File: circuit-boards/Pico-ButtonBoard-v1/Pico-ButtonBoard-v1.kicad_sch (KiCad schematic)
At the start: 16 parts, among them J17 CAN, J18 CAN, J19 BATT, J22 DC_IN, U3 MCP2518FDT-H/SL, U4 MCP2558FD, U5 4.0 MHz

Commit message: Update footprints
Signed-off-by: Scott Berman <sgberman1@gmail.com>
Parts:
- TP101: renamed from TP1; footprint (none) -> TestPoint:TestPoint_Keystone_5000-5004_Miniature; now not fitted
- TP102: renamed from TP2; footprint (none) -> TestPoint:TestPoint_Keystone_5000-5004_Miniature; now not fitted
- U101: renamed from U5; footprint (none) -> Pico-ButtonBoard:Wurth-CFPS-73
- renumbered A1 to A101, C19 to C101, C23 to C102, C20 to C103, C21 to C104, C22 to C105, J22 to J101, J19 to J102, J17 to J103, J18 to J104, R49 to R101, U3 to U102, U4 to U103
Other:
- title: (none) -> Pico Button Board

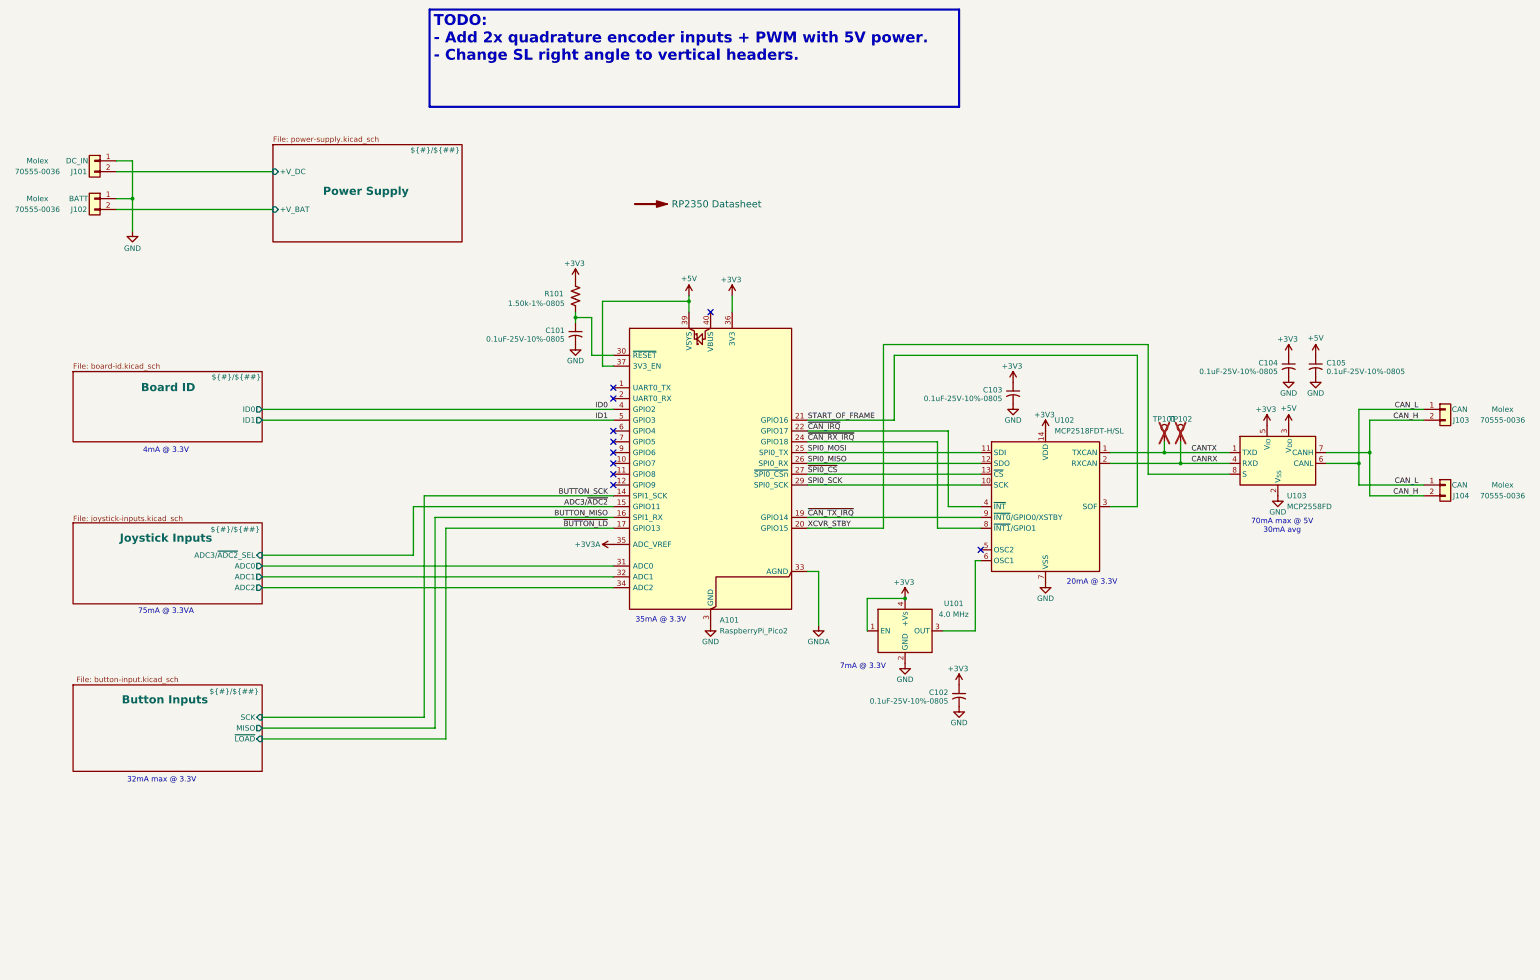
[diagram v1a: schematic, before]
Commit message: Pico Button Board initial placement
Signed-off-by: Scott Berman <sgberman1@gmail.com>
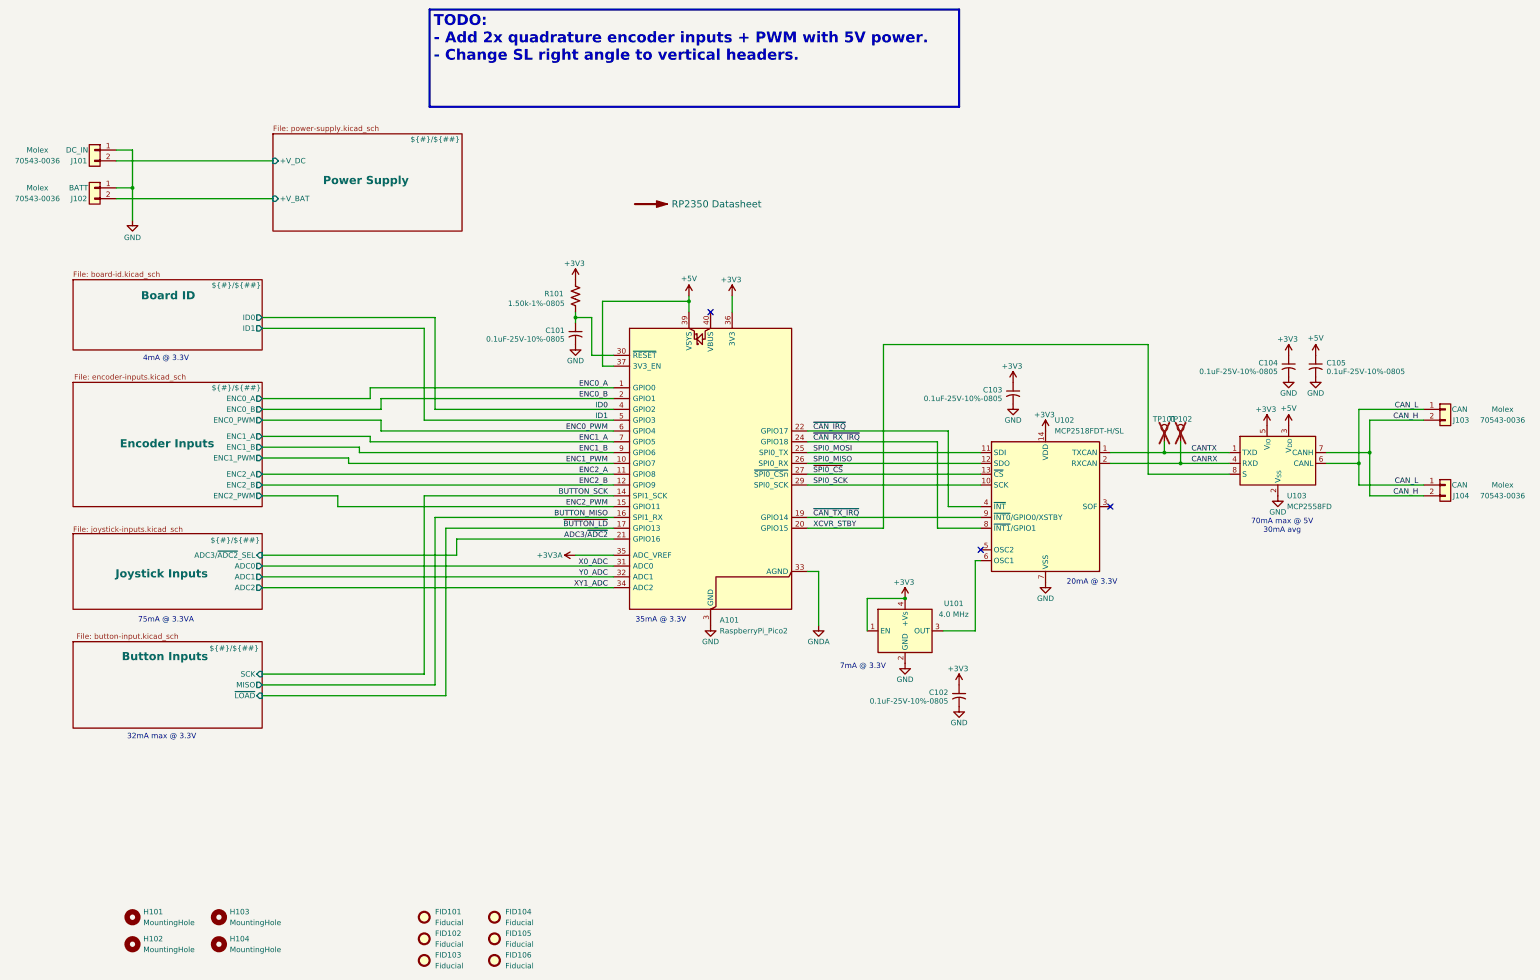
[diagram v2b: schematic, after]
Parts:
- added FID101, FID102, FID103, FID104, FID105, FID106: Fiducial, Fiducial:Fiducial_Cross_1.5mm_Mask2mm, symbol Mechanical:Fiducial
- added H101, H102, H103, H104: MountingHole, MountingHole:MountingHole_3.2mm_M3, symbol Mechanical:MountingHole
- C101, C102, C103, C104, C105: LCSC Part # C519981 -> (none)
- J101, J102, J103, J104: footprint Pico-ButtonBoard:Molex-70555-0036 -> Pico-ButtonBoard:Molex-70543-0001; DIST P/N WM4175-ND -> WM4824-ND; MFG P/N 70555-0036 -> 70543-0036
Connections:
- net ADC3/~{ADC2}: now also A101.21 (GPIO16); no longer A101.15 (GPIO11)
- net ENC0_A: now reaches A101.1 (GPIO0)
- net ENC1_PWM: now reaches A101.10 (GPIO7)
- net ENC2_A: now reaches A101.11 (GPIO8)
- net ENC2_B: now reaches A101.12 (GPIO9)
- net ENC0_B: now reaches A101.2 (GPIO1)
- net ENC0_PWM: now reaches A101.6 (GPIO4)
- net ENC1_A: now reaches A101.7 (GPIO5)
- net ENC1_B: now reaches A101.9 (GPIO6)
- net Joystick Inputs/ADC0 renamed X0_ADC
- net Joystick Inputs/ADC1 renamed Y0_ADC
- net Joystick Inputs/ADC2 renamed XY1_ADC
- net START_OF_FRAME: no longer names the net of U102.3 (CLKO/SOF)
- net START_OF_FRAME: no longer A101.21 (GPIO16)
- new net ENC2_PWM: A101.15 (GPIO11)
- no-connect marks 10 -> 3
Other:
- added sheet Encoder Inputs (encoder-inputs.kicad_sch)
- moved on the sheet: J101, J102

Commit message: Pico Button Board initial pcb checkin
Signed-off-by: Scott Berman <sgberman1@gmail.com>
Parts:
- A1: renamed from A101; footprint Module:RaspberryPi_Pico_Common_Unspecified -> Pico-ButtonBoard:RaspberryPi_Pico_Common_Unspecified
- FID1: renamed from FID105; footprint Fiducial:Fiducial_Cross_1.5mm_Mask2mm -> Pico-ButtonBoard:Fiducial_1.6mm_Mask3mm
- FID2: renamed from FID103; footprint Fiducial:Fiducial_Cross_1.5mm_Mask2mm -> Pico-ButtonBoard:Fiducial_1.6mm_Mask3mm
- FID3: renamed from FID101; footprint Fiducial:Fiducial_Cross_1.5mm_Mask2mm -> Pico-ButtonBoard:Fiducial_1.6mm_Mask3mm
- FID4: renamed from FID102; footprint Fiducial:Fiducial_Cross_1.5mm_Mask2mm -> Pico-ButtonBoard:Fiducial_1.6mm_Mask3mm
- FID5: renamed from FID104; footprint Fiducial:Fiducial_Cross_1.5mm_Mask2mm -> Pico-ButtonBoard:Fiducial_1.6mm_Mask3mm
- FID6: renamed from FID106; footprint Fiducial:Fiducial_Cross_1.5mm_Mask2mm -> Pico-ButtonBoard:Fiducial_1.6mm_Mask3mm
- renumbered C104 to C20, C105 to C22, C103 to C23, C101 to C26, C102 to C4, H101 to H1, H102 to H2, H104 to H3, H103 to H4, J104 to J19, J103 to J20, J102 to J21, J101 to J22, R101 to R59, TP101 to TP4, TP102 to TP5, U101 to U4, U102 to U5, U103 to U8
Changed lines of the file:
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@@
 		)
 	)
-	(text_box "TODO:\n- Add 2x quadrature encoder inputs + PWM with 5V power.\n- Change SL right angle to vertical headers."
-		(exclude_from_sim no)
-		(at 138.43 27.94 0)
-		(size 124.46 22.86)
-		(margins 0.9525 0.9525 0.9525 0.9525)
-		(stroke
-			(width 0.508)
-			(type solid)
-			(color 255 0 0 1)
-		)
-		(fill
-			(type none)
-		)
-		(effects
-			(font
-				(size 2.54 2.54)
-				(thickness 0.508)
-				(bold yes)
-				(color 255 0 0 1)
-			)
-			(justify left top)
-		)
-	)
 	(junction
 		(at 250.19 166.37)
@@
 		(dnp no)
 		(fields_autoplaced yes)
-		(property "Reference" "H103"
+		(property "Reference" "H4"
 			(at 91.44 240.0299 0)
 			(effects
@@
 			(project "Pico-ButtonBoard-v1"
 				(path "/644201a9-3a2f-4df3-9c93-2ae55394df4b"
-					(reference "H103")
+					(reference "H4")
 					(unit 1)
 				)
@@
 		(dnp no)
 		(fields_autoplaced yes)
-		(property "Reference" "FID103"
+		(property "Reference" "FID2"
 			(at 139.7 250.1899 0)
 			(effects
@@
 			)
 		)
-		(property "Footprint" "Fiducial:Fiducial_Cross_1.5mm_Mask2mm"
+		(property "Footprint" "Pico-ButtonBoard:Fiducial_1.6mm_Mask3mm"
 			(at 137.16 251.46 0)
 			(effects
@@
 			(project "Pico-ButtonBoard-v1"
 				(path "/644201a9-3a2f-4df3-9c93-2ae55394df4b"
-					(reference "FID103")
+					(reference "FID2")
 					(unit 1)
 				)
@@
 		(dnp no)
 		(fields_autoplaced yes)
-		(property "Reference" "FID104"
+		(property "Reference" "FID5"
 			(at 156.21 240.0299 0)
 			(effects
@@
 			)
 		)
-		(property "Footprint" "Fiducial:Fiducial_Cross_1.5mm_Mask2mm"
+		(property "Footprint" "Pico-ButtonBoard:Fiducial_1.6mm_Mask3mm"
 			(at 153.67 241.3 0)
 			(effects
@@
 			(project "Pico-ButtonBoard-v1"
 				(path "/644201a9-3a2f-4df3-9c93-2ae55394df4b"
-					(reference "FID104")
+					(reference "FID5")
 					(unit 1)
 				)
@@
 		(on_board yes)
 		(dnp no)
-		(property "Reference" "C104"
+		(property "Reference" "C20"
 			(at 337.82 110.998 0)
 			(effects
@@
 			(project "Pico-ButtonBoard-v1"
 				(path "/644201a9-3a2f-4df3-9c93-2ae55394df4b"
-					(reference "C104")
+					(reference "C20")
 					(unit 1)
 				)
@@
 		(dnp no)
 		(fields_autoplaced yes)
-		(property "Reference" "FID102"
+		(property "Reference" "FID4"
 			(at 139.7 245.1099 0)
 			(effects
@@
 			)
 		)
-		(property "Footprint" "Fiducial:Fiducial_Cross_1.5mm_Mask2mm"
+		(property "Footprint" "Pico-ButtonBoard:Fiducial_1.6mm_Mask3mm"
 			(at 137.16 246.38 0)
 			(effects
@@
 			(project "Pico-ButtonBoard-v1"
 				(path "/644201a9-3a2f-4df3-9c93-2ae55394df4b"
-					(reference "FID102")
+					(reference "FID4")
 					(unit 1)
 				)
@@
 		(on_board yes)
 		(dnp no)
-		(property "Reference" "J101"
+		(property "Reference" "J22"
 			(at 57.912 63.5 0)
 			(effects
@@
 			(project "Pico-ButtonBoard-v1"
 				(path "/644201a9-3a2f-4df3-9c93-2ae55394df4b"
-					(reference "J101")
+					(reference "J22")
 					(unit 1)
 				)
@@
 		(dnp no)
 		(fields_autoplaced yes)
-		(property "Reference" "FID105"
+		(property "Reference" "FID1"
 			(at 156.21 245.1099 0)
 			(effects
@@
 			)
 		)
-		(property "Footprint" "Fiducial:Fiducial_Cross_1.5mm_Mask2mm"
+		(property "Footprint" "Pico-ButtonBoard:Fiducial_1.6mm_Mask3mm"
 			(at 153.67 246.38 0)
 			(effects
@@
 			(project "Pico-ButtonBoard-v1"
 				(path "/644201a9-3a2f-4df3-9c93-2ae55394df4b"
-					(reference "FID105")
+					(reference "FID1")
 					(unit 1)
 				)
@@
 		(dnp no)
 		(fields_autoplaced yes)
-		(property "Reference" "H104"
+		(property "Reference" "H3"
 			(at 91.44 246.3799 0)
 			(effects
@@
 			(project "Pico-ButtonBoard-v1"
 				(path "/644201a9-3a2f-4df3-9c93-2ae55394df4b"
-					(reference "H104")
+					(reference "H3")
 					(unit 1)
 				)
@@
 		(dnp no)
 		(fields_autoplaced yes)
-		(property "Reference" "A101"
+		(property "Reference" "A1"
 			(at 206.6133 171.45 0)
 			(effects
@@
 			)
 		)
-		(property "Footprint" "Module:RaspberryPi_Pico_Common_Unspecified"
+		(property "Footprint" "Pico-ButtonBoard:RaspberryPi_Pico_Common_Unspecified"
 			(at 204.47 184.15 0)
 			(effects
@@
 			(project ""
 				(path "/644201a9-3a2f-4df3-9c93-2ae55394df4b"
-					(reference "A101")
+					(reference "A1")
 					(unit 1)
 				)
@@
 		(on_board yes)
 		(dnp no)
-		(property "Reference" "J103"
+		(property "Reference" "J20"
 			(at 378.968 124.46 0)
 			(effects
@@
 			(project "Pico-ButtonBoard-v1"
 				(path "/644201a9-3a2f-4df3-9c93-2ae55394df4b"
-					(reference "J103")
+					(reference "J20")
 					(unit 1)
 				)
@@
 		(on_board yes)
 		(dnp no)
-		(property "Reference" "C105"
+		(property "Reference" "C22"
 			(at 349.25 110.998 0)
 			(effects
@@
 			(project "Pico-ButtonBoard-v1"
 				(path "/644201a9-3a2f-4df3-9c93-2ae55394df4b"
-					(reference "C105")
+					(reference "C22")
 					(unit 1)
 				)
@@
 		(on_board yes)
 		(dnp no)
-		(property "Reference" "R101"
+		(property "Reference" "R59"
 			(at 169.926 94.742 0)
 			(effects
@@
 			(project "Pico-ButtonBoard-v1"
 				(path "/644201a9-3a2f-4df3-9c93-2ae55394df4b"
-					(reference "R101")
+					(reference "R59")
 					(unit 1)
 				)
@@
 		(on_board yes)
 		(dnp no)
-		(property "Reference" "C101"
+		(property "Reference" "C26"
 			(at 170.18 103.378 0)
 			(effects
@@
 			(project "Pico-ButtonBoard-v1"
 				(path "/644201a9-3a2f-4df3-9c93-2ae55394df4b"
-					(reference "C101")
+					(reference "C26")
 					(unit 1)
 				)
@@
 		(dnp no)
 		(fields_autoplaced yes)
-		(property "Reference" "U101"
+		(property "Reference" "U4"
 			(at 261.62 167.5698 0)
 			(effects
@@
 			(project ""
 				(path "/644201a9-3a2f-4df3-9c93-2ae55394df4b"
-					(reference "U101")
+					(reference "U4")
 					(unit 1)
 				)
@@
 		(dnp no)
 		(fields_autoplaced yes)
-		(property "Reference" "FID101"
+		(property "Reference" "FID3"
 			(at 139.7 240.0299 0)
 			(effects
@@
 			)
 		)
-		(property "Footprint" "Fiducial:Fiducial_Cross_1.5mm_Mask2mm"
+		(property "Footprint" "Pico-ButtonBoard:Fiducial_1.6mm_Mask3mm"
 			(at 137.16 241.3 0)
 			(effects
@@
 			(project ""
 				(path "/644201a9-3a2f-4df3-9c93-2ae55394df4b"
-					(reference "FID101")
+					(reference "FID3")
 					(unit 1)
 				)
@@
 		(on_board yes)
 		(dnp no)
-		(property "Reference" "J104"
+		(property "Reference" "J19"
 			(at 378.968 142.24 0)
 			(effects
@@
 			(project "Pico-ButtonBoard-v1"
 				(path "/644201a9-3a2f-4df3-9c93-2ae55394df4b"
-					(reference "J104")
+					(reference "J19")
 					(unit 1)
 				)
@@
 		(dnp no)
 		(fields_autoplaced yes)
-		(property "Reference" "H101"
+		(property "Reference" "H1"
 			(at 71.12 240.0299 0)
 			(effects
@@
 			(project ""
 				(path "/644201a9-3a2f-4df3-9c93-2ae55394df4b"
-					(reference "H101")
+					(reference "H1")
 					(unit 1)
 				)
@@
 		(on_board yes)
 		(dnp no)
-		(property "Reference" "C103"
+		(property "Reference" "C23"
 			(at 273.05 117.348 0)
 			(effects
@@
 			(project "Pico-ButtonBoard-v1"
 				(path "/644201a9-3a2f-4df3-9c93-2ae55394df4b"
-					(reference "C103")
+					(reference "C23")
 					(unit 1)
 				)
@@
 		(on_board yes)
 		(dnp no)
-		(property "Reference" "J102"
+		(property "Reference" "J21"
 			(at 57.912 72.39 0)
 			(effects
@@
 			(project "Pico-ButtonBoard-v1"
 				(path "/644201a9-3a2f-4df3-9c93-2ae55394df4b"
-					(reference "J102")
+					(reference "J21")
 					(unit 1)
 				)
@@
 		(on_board yes)
 		(dnp no)
-		(property "Reference" "C102"
+		(property "Reference" "C4"
 			(at 260.35 188.468 0)
 			(effects
@@
 			(project "Pico-ButtonBoard-v1"
 				(path "/644201a9-3a2f-4df3-9c93-2ae55394df4b"
-					(reference "C102")
+					(reference "C4")
 					(unit 1)
 				)
@@
 		(dnp no)
 		(fields_autoplaced yes)
-		(property "Reference" "U102"
+		(property "Reference" "U5"
 			(at 285.3533 124.46 0)
 			(effects
@@
 			(project ""
 				(path "/644201a9-3a2f-4df3-9c93-2ae55394df4b"
-					(reference "U102")
+					(reference "U5")
 					(unit 1)
 				)
@@
 		(dnp no)
 		(fields_autoplaced yes)
-		(property "Reference" "FID106"
+		(property "Reference" "FID6"
 			(at 156.21 250.1899 0)
 			(effects
@@
 			)
 		)
-		(property "Footprint" "Fiducial:Fiducial_Cross_1.5mm_Mask2mm"
+		(property "Footprint" "Pico-ButtonBoard:Fiducial_1.6mm_Mask3mm"
 			(at 153.67 251.46 0)
 			(effects
@@
 			(project "Pico-ButtonBoard-v1"
 				(path "/644201a9-3a2f-4df3-9c93-2ae55394df4b"
-					(reference "FID106")
+					(reference "FID6")
 					(unit 1)
 				)
@@
 		(dnp no)
 		(fields_autoplaced yes)
-		(property "Reference" "H102"
+		(property "Reference" "H2"
 			(at 71.12 246.3799 0)
 			(effects
@@
 			(project "Pico-ButtonBoard-v1"
 				(path "/644201a9-3a2f-4df3-9c93-2ae55394df4b"
-					(reference "H102")
+					(reference "H2")
 					(unit 1)
 				)
@@
 		(on_board yes)
 		(dnp yes)
-		(property "Reference" "TP102"
+		(property "Reference" "TP5"
 			(at 314.96 124.206 0)
 			(effects
@@
 			(project "Pico-ButtonBoard-v1"
 				(path "/644201a9-3a2f-4df3-9c93-2ae55394df4b"
-					(reference "TP102")
+					(reference "TP5")
 					(unit 1)
 				)
@@
 		(on_board yes)
 		(dnp yes)
-		(property "Reference" "TP101"
+		(property "Reference" "TP4"
 			(at 311.15 124.206 0)
 			(effects
@@
 			(project ""
 				(path "/644201a9-3a2f-4df3-9c93-2ae55394df4b"
-					(reference "TP101")
+					(reference "TP4")
 					(unit 1)
 				)
@@
 		(dnp no)
 		(fields_autoplaced yes)
-		(property "Reference" "U103"
+		(property "Reference" "U8"
 			(at 339.9633 142.24 0)
 			(effects
@@
 			(project ""
 				(path "/644201a9-3a2f-4df3-9c93-2ae55394df4b"
-					(reference "U103")
+					(reference "U8")
 					(unit 1)
 				)

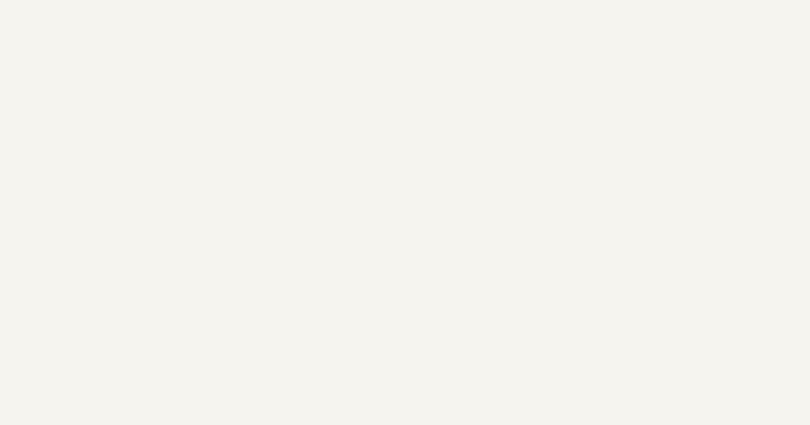
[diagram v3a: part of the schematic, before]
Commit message: Update Pico Button Board Layout
Signed-off-by: Scott Berman <sgberman1@gmail.com>
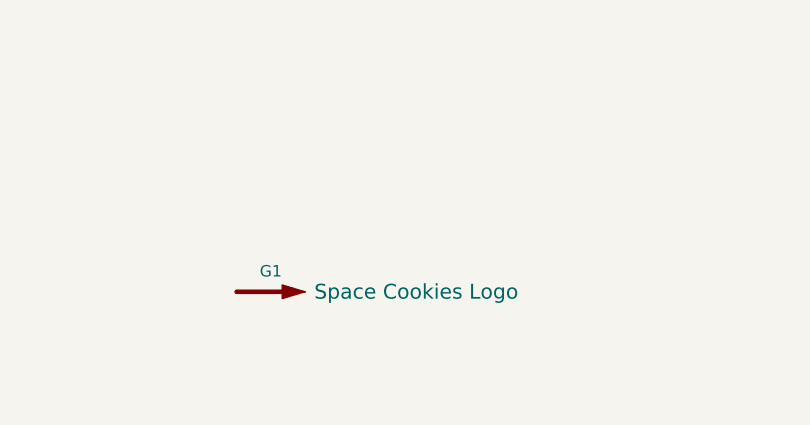
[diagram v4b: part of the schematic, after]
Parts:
- added G1: Space Cookies Logo, Pico-ButtonBoard:SPACE_COOKIES_LOGO_7mm, symbol Graphic:SYM_Arrow_Large
- A1: DIST (none) -> Digikey; DIST P/N (none) -> 2648-SC1632-ND; MFG (none) -> Raspberry PI; MFG P/N (none) -> SC1632
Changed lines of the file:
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@@
 	(title_block
 		(title "Pico Button Board")
-		(date "2025-12-25")
+		(date "2025-12-28")
 		(rev "1")
 	)
@@
 			)
 		)
+		(property "MFG" "Raspberry PI"
+			(at 204.47 137.16 0)
+			(effects
+				(font
+					(size 1.27 1.27)
+				)
+				(hide yes)
+			)
+		)
+		(property "MFG P/N" "SC1632"
+			(at 204.47 137.16 0)
+			(effects
+				(font
+					(size 1.27 1.27)
+				)
+				(hide yes)
+			)
+		)
+		(property "DIST" "Digikey"
+			(at 204.47 137.16 0)
+			(effects
+				(font
+					(size 1.27 1.27)
+				)
+				(hide yes)
+			)
+		)
+		(property "DIST P/N" "2648-SC1632-ND"
+			(at 204.47 137.16 0)
+			(effects
+				(font
+					(size 1.27 1.27)
+				)
+				(hide yes)
+			)
+		)
 		(pin "11"
 		)
@@
 					(unit 1)
 				)
+			)
+		)
+	)
+	(symbol
+		(lib_id "Graphic:SYM_Arrow_Large")
+		(at 200.66 241.3 0)
+		(unit 1)
+		(exclude_from_sim no)
+		(in_bom no)
+		(on_board yes)
+		(dnp no)
+		(property "Reference" "G1"
+			(at 200.66 239.014 0)
+			(effects
+				(font
+					(size 1.27 1.27)
+				)
+			)
+		)
+		(property "Value" "Space Cookies Logo"
+			(at 205.486 241.3 0)
+			(effects
+				(font
+					(size 1.651 1.651)
+				)
+				(justify left)
+			)
+		)
+		(property "Footprint" "Pico-ButtonBoard:SPACE_COOKIES_LOGO_7mm"
+			(at 200.66 241.3 0)
+			(effects
+				(font
+					(size 1.27 1.27)
+				)
+				(hide yes)
+			)
+		)
+		(property "Datasheet" ""
+			(at 200.66 241.3 0)
+			(effects
+				(font
+					(size 1.27 1.27)
+				)
+				(hide yes)
+			)
+		)
+		(property "Description" "Filled arrow, 300mil"
+			(at 200.66 241.3 0)
+			(effects
+				(font
+					(size 1.27 1.27)
+				)
+				(hide yes)
+			)
+		)
+		(instances
+			(project "Pico-ButtonBoard-v1"
+				(path "/644201a9-3a2f-4df3-9c93-2ae55394df4b"
+					(reference "G1")
+					(unit 1)
+				)
